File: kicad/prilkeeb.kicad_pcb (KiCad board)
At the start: 2 copper layers, 162.4 x 143.1 mm, 71 parts, among them U2 Nice_Nano_V2

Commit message: Update layout
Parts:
- added REF**: Stabilizer_MX_2.00u, ScottoKeebs_Stabilizer:Stabilizer_MX_2.00u, F.Cu at (142.2, 156.1)
- D1, D10, D11, D12, D13, D14, D15, D16, D17, D18, D19, D2, D20, D21, D22, D23, D24, D25, D26, D27, D28, D29, D3, D30, D31, D32, D33, D34, D35, D4, D5, D6, D7, D8, D9: moved to B.Cu
- moved S33 48.0 mm to (142.2, 156.1), turned to -30 degrees
- moved D33 44.1 mm to (158.9, 178.7), turned to 60 degrees
- moved S35 39.7 mm to (156.0, 173.5), turned to -30 degrees
- moved D32 28.8 mm to (121.3, 159.9), turned to 60 degrees
- moved S32 25.6 mm to (118.4, 154.8), turned to -30 degrees
- moved D34 20.4 mm to (168.4, 162.2), turned to 60 degrees
- moved S19 19.1 mm to (38.1, 104.8), turned to 0 degrees
- moved S20 19.1 mm to (57.1, 104.8), turned to 0 degrees
- moved S12 19.0 mm to (38.1, 85.7), turned to 0 degrees
- moved S13 19.0 mm to (57.1, 85.7), turned to 0 degrees
- moved S26 19.0 mm to (38.1, 123.8), turned to 0 degrees
- moved S27 19.0 mm to (57.1, 123.8), turned to 0 degrees
- moved S29 19.0 mm to (38.1, 142.9), turned to 0 degrees
- moved S30 19.0 mm to (57.1, 142.9), turned to 0 degrees
- moved S31 19.0 mm to (76.2, 142.9), turned to 0 degrees
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- renumbered S3 to S1, S12 to S10, S13 to S11, S8 to S12, S9 to S13, S17 to S15, S18 to S16, S19 to S17, S20 to S18, S15 to S19, S4 to S2, S16 to S20, S24 to S22, S25 to S23, S26 to S24, S27 to S25, S22 to S26, S23 to S27, S5 to S3, S35 to S33, S33 to S35, S6 to S4, S1 to S5, S2 to S6, S10 to S8, S11 to S9
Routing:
- net Col_1: track 247.7 -> 0.00 mm
- net Col_2: track 226.2 -> 0.00 mm
- net Row_5: track 210.0 -> 0.00 mm
- net Col_4: track 200.5 -> 0.00 mm
- net Col_5: track 167.3 -> 0.00 mm
- net Col_3: track 208.5 -> 44.4 mm
- net Row_2: track 151.8 -> 0.00 mm
- net Row_4: track 190.9 -> 45.1 mm
- net Col_6: track 142.6 -> 0.00 mm
- net Row_1: track 138.9 -> 0.00 mm
- net Row_3: track 172.5 -> 36.4 mm
- net Col_7: track 104.9 -> 0.00 mm
- net Net-(D12-A): track 14.1 -> 0.00 mm
- net Net-(D22-A): track 12.4 -> 0.00 mm
- net Net-(D1-A): track 12.3 -> 0.00 mm
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
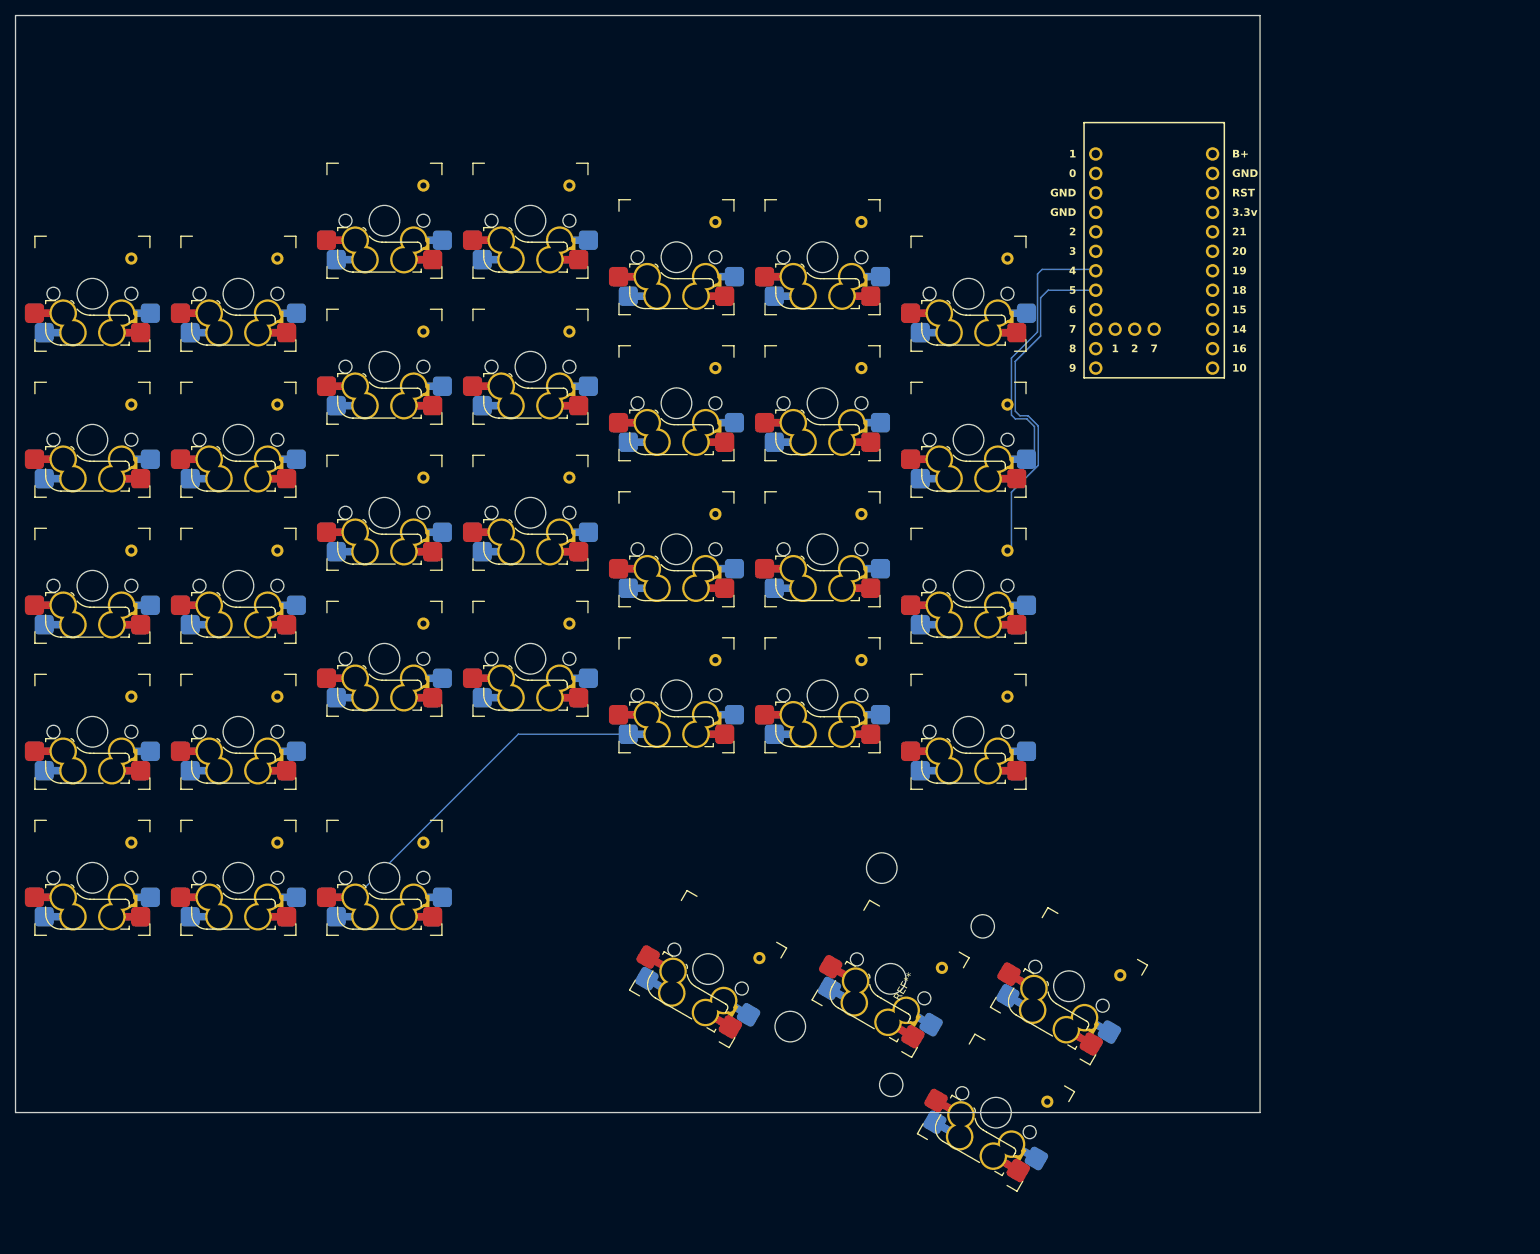
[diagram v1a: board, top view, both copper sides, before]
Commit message: Update placement and basice routing
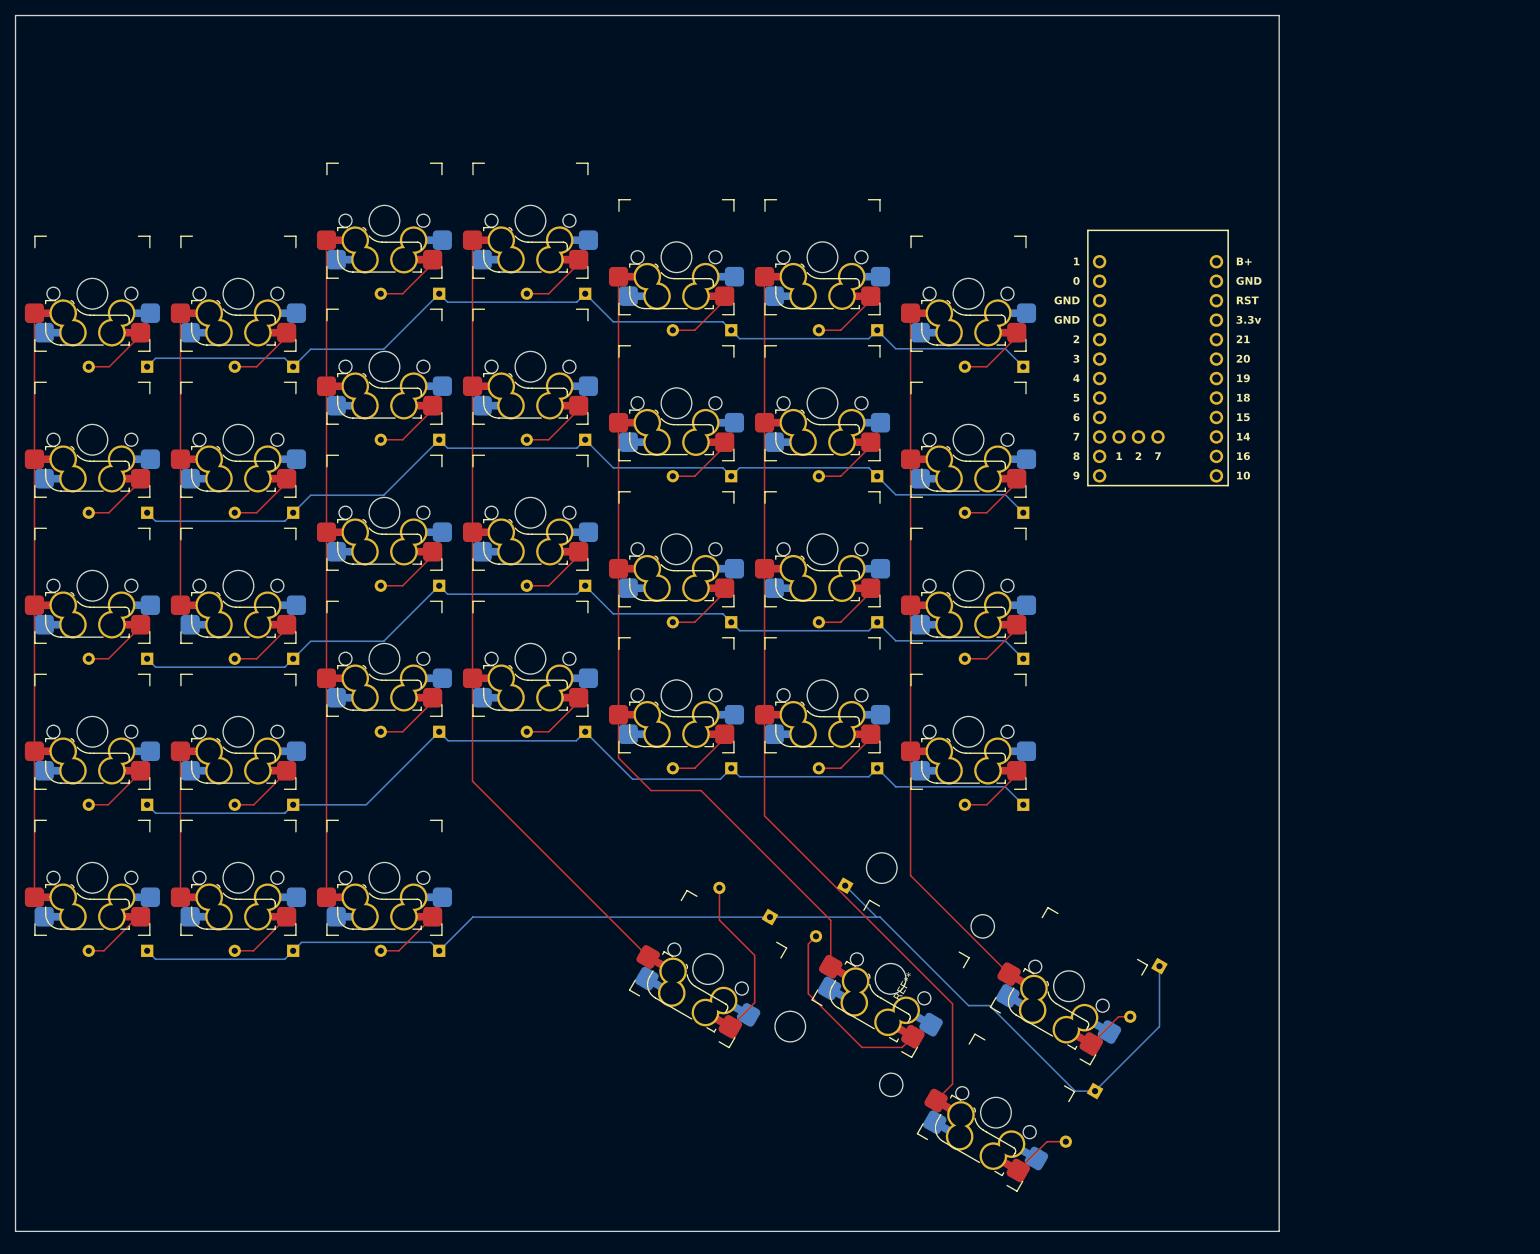
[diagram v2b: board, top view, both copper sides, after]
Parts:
- moved D35 41.5 mm to (136.3, 143.9), turned to -120 degrees
- moved D34 32.9 mm to (177.3, 154.4), turned to -120 degrees
- moved S34 23.3 mm to (165.5, 157.0)
- moved S33 22.2 mm to (142.2, 156.1)
- moved S35 19.1 mm to (156.0, 173.5)
- moved U2 14.1 mm to (177.1, 76.2)
- moved D32 13.0 mm to (126.5, 148.0), turned to 150 degrees
- moved D33 8.53 mm to (168.9, 170.7), turned to -120 degrees
- moved D2 6.81 mm to (64.3, 76.2), turned to 180 degrees
- moved D30 6.81 mm to (64.3, 152.4), turned to 180 degrees
- moved D9 6.81 mm to (64.3, 95.2), turned to 180 degrees
- moved D14 6.81 mm to (159.5, 95.2), turned to 180 degrees
- moved D17 6.81 mm to (83.3, 104.8), turned to 180 degrees
- moved D18 6.81 mm to (102.4, 104.8), turned to 180 degrees
- moved D24 6.81 mm to (83.3, 123.8), turned to 180 degrees
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- renumbered D34 to D33, D35 to D34, D33 to D35, S35 to S33, S33 to S34, S34 to S35
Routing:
- net Row_5: track 0.00 -> 162.3 mm
- net Row_1: track 0.00 -> 125.3 mm
- net Row_2: track 0.00 -> 124.9 mm
- net Col_6: track 0.00 -> 119.3 mm
- net Col_5: track 0.00 -> 106.9 mm
- net Col_4: track 0.00 -> 103.0 mm
- net Col_7: track 0.00 -> 91.5 mm
- net Row_3: track 36.4 -> 124.9 mm
- net Row_4: track 45.1 -> 126.2 mm
- net Col_1: track 0.00 -> 76.2 mm
- net Col_2: track 0.00 -> 57.1 mm
- net Col_3: track 44.4 -> 85.7 mm
- net Net-(D35-A): track 0.00 -> 25.6 mm
- net Net-(D32-A): track 0.00 -> 21.4 mm
- net Net-(D29-A): track 0.00 -> 14.1 mm
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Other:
- board size 162.4 x 143.1 mm -> 164.9 x 158.6 mm

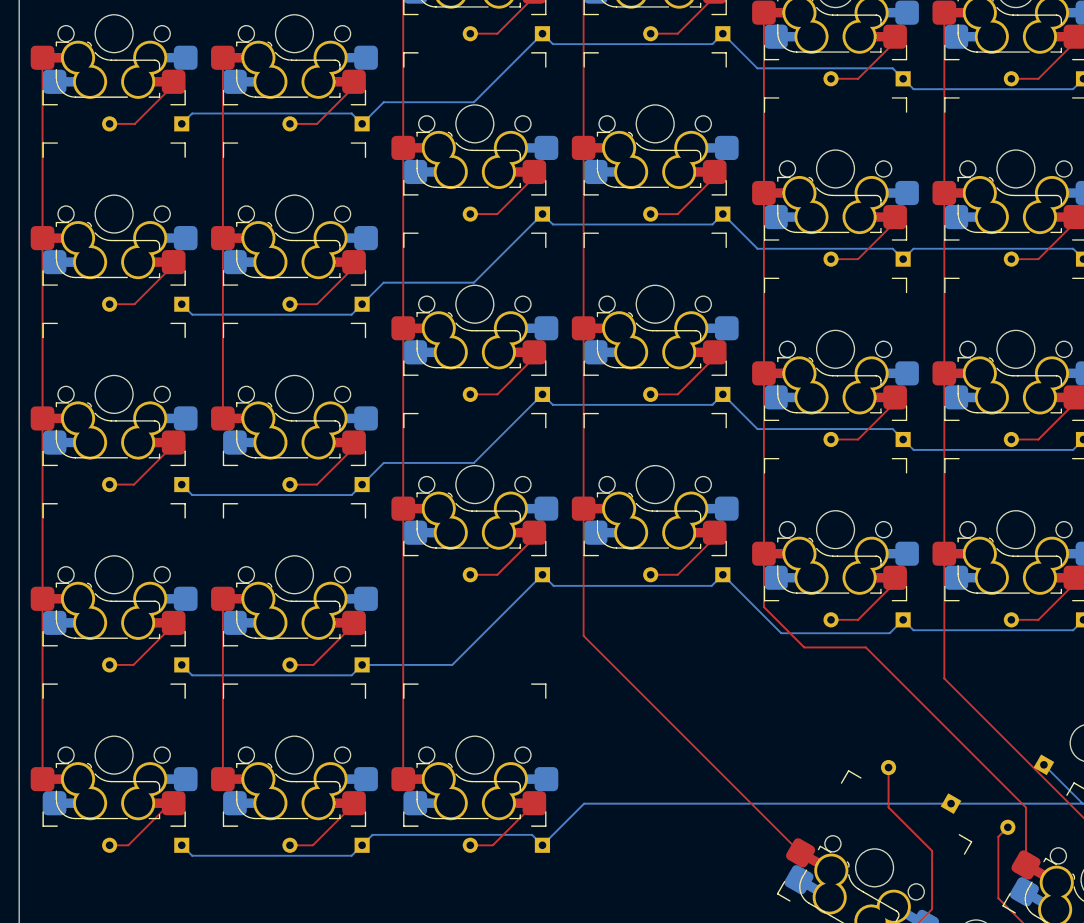
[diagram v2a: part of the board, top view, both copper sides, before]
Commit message: Update project name
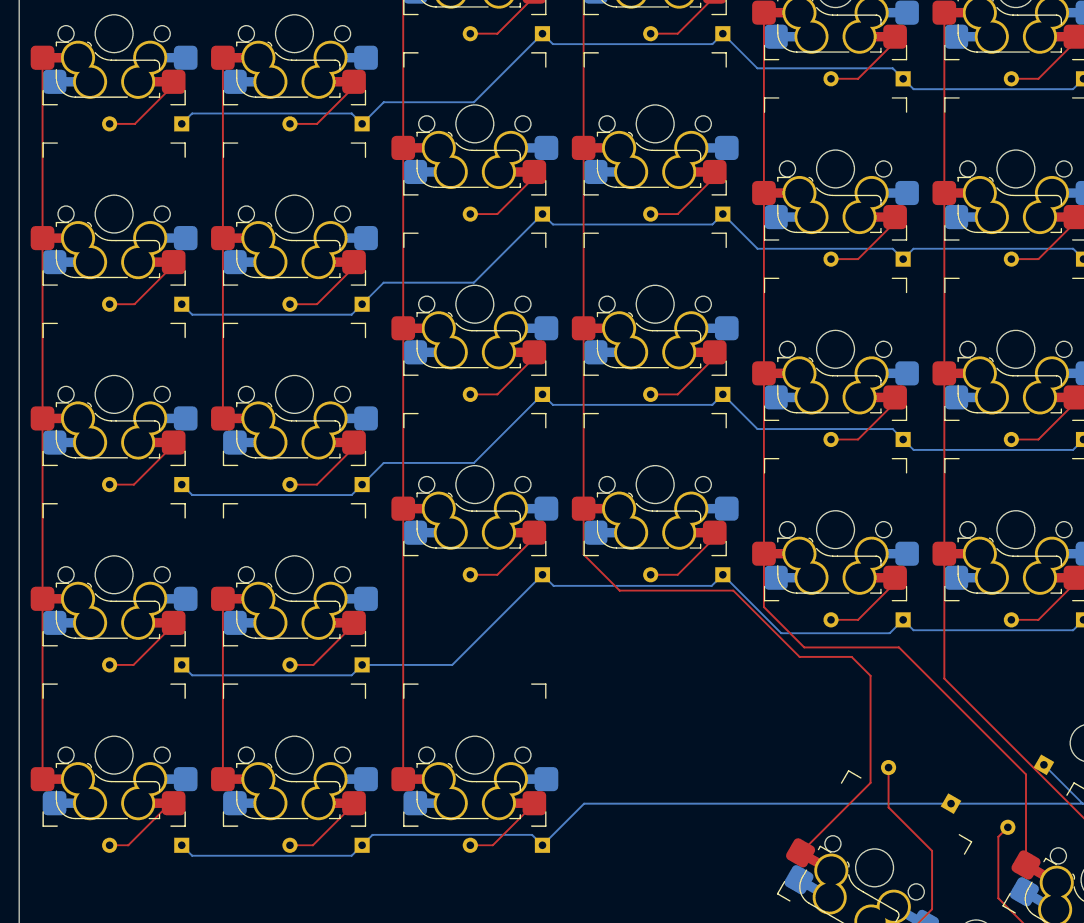
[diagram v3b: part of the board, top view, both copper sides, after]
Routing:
- net Col_4: track 103.0 -> 119.4 mm
- net Col_5: track 106.9 -> 108.9 mm
- net Col_1: track 76.2 -> 77.9 mm
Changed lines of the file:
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@@
+	)
+	(segment
+		(start 30.54 69.215)
+		(end 32.285 69.215)
+		(width 0.2)
+		(layer "F.Cu")
+		(net 41)
 	)
 	(segment
@@
 	)
 	(segment
-		(start 87.69 130.283661)
-		(end 110.607294 153.200955)
+		(start 103.5 125.5)
+		(end 110.5 132.5)
 		(width 0.2)
 		(layer "F.Cu")
@@
 	)
 	(segment
+		(start 87.69 121.69)
+		(end 91.5 125.5)
+		(width 0.2)
+		(layer "F.Cu")
+		(net 44)
+	)
+	(segment
+		(start 87.69 116.84)
+		(end 87.69 121.69)
+		(width 0.2)
+		(layer "F.Cu")
+		(net 44)
+	)
+	(segment
+		(start 91.5 125.5)
+		(end 103.5 125.5)
+		(width 0.2)
+		(layer "F.Cu")
+		(net 44)
+	)
+	(segment
 		(start 87.69 59.69)
 		(end 87.69 78.74)
@@
 	)
 	(segment
-		(start 87.69 116.84)
-		(end 87.69 130.283661)
+		(start 116 132.5)
+		(end 118 134.5)
+		(width 0.2)
+		(layer "F.Cu")
+		(net 44)
+	)
+	(segment
+		(start 110.5 132.5)
+		(end 116 132.5)
+		(width 0.2)
+		(layer "F.Cu")
+		(net 44)
+	)
+	(segment
+		(start 118 134.5)
+		(end 118 145.808249)
+		(width 0.2)
+		(layer "F.Cu")
+		(net 44)
+	)
+	(segment
+		(start 118 145.808249)
+		(end 110.607294 153.200955)
 		(width 0.2)
 		(layer "F.Cu")
@@
 	)
 	(segment
-		(start 117.5 131.5)
-		(end 134.419794 148.419794)
-		(width 0.2)
-		(layer "F.Cu")
-		(net 45)
-	)
-	(segment
-		(start 134.419794 148.419794)
-		(end 134.419794 154.477063)
-		(width 0.2)
-		(layer "F.Cu")
-		(net 45)
-	)
-	(segment
-		(start 111 131.5)
-		(end 117.5 131.5)
+		(start 121 131.5)
+		(end 134.419794 144.919794)
 		(width 0.2)
 		(layer "F.Cu")
@@
 		(width 0.2)
 		(layer "F.Cu")
+		(net 45)
+	)
+	(segment
+		(start 111 131.5)
+		(end 121 131.5)
+		(width 0.2)
+		(layer "F.Cu")
+		(net 45)
+	)
+	(segment
+		(start 134.419794 144.919794)
+		(end 134.419794 154.477063)
+		(width 0.2)
+		(layer "F.Cu")

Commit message: Acceptable tracks
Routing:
- net Col_2: track 57.1 -> 240.0 mm
- net Col_1: track 77.9 -> 259.5 mm
- net Col_3: track 85.7 -> 226.6 mm
- net Row_5: track 162.3 -> 286.7 mm
- net Col_4: track 119.4 -> 232.5 mm
- net Col_5: track 108.9 -> 210.9 mm
- net Col_6: track 119.3 -> 208.6 mm
- net Col_7: track 91.5 -> 167.7 mm
- net Row_4: track 126.2 -> 194.4 mm
- net Row_3: track 124.9 -> 175.5 mm
- net Row_2: track 124.9 -> 161.1 mm
- net Row_1: track 125.3 -> 136.8 mm
- net Net-(D34-A): track 6.56 -> 3.55 mm

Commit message: Nearly finish the routing
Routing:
- net Row_2: track 161.1 -> 175.6 mm
- net Col_6: track 208.6 -> 222.7 mm, vias 0 -> 2
- net Row_1: track 136.8 -> 147.9 mm
- net Col_4: track 232.5 -> 223.5 mm, vias 0 -> 2
- net Row_4: track 194.4 -> 185.9 mm
- net Col_3: track 226.6 -> 219.5 mm, vias 0 -> 1
- net Col_5: track 210.9 -> 217.6 mm, vias 0 -> 4
- net Col_2: track 240.0 -> 235.3 mm, vias 0 -> 1
- net Row_5: track 286.7 -> 282.6 mm, vias 0 -> 3
- net Col_1: track 259.5 -> 256.1 mm, vias 0 -> 1
- net Row_3: track 175.5 -> 178.0 mm

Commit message: Update layout
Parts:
- added REF**: Stabilizer_MX_2.00u, ScottoKeebs_Stabilizer:Stabilizer_MX_2.00u, F.Cu at (176.6, 167.2)
- moved D33 40.4 mm to (148.1, 136.0), turned to 180 degrees
- moved D34 25.5 mm to (159.6, 136.0), turned to 180 degrees
- moved U2 21.0 mm to (198.1, 76.1)
- moved S11 19.1 mm to (152.4, 81.0)
- moved S18 19.1 mm to (152.4, 100.0)
- moved S25 19.1 mm to (152.4, 119.1)
- moved S4 19.1 mm to (152.4, 61.9)
- moved S13 19.1 mm to (76.2, 85.7)
- moved S20 19.1 mm to (76.2, 104.8)
- moved S27 19.1 mm to (76.2, 123.8)
- moved S30 19.1 mm to (76.2, 142.9)
- moved S6 19.1 mm to (76.2, 66.7)
- moved S1 19.0 mm to (95.2, 57.1)
- moved S10 19.0 mm to (133.3, 81.0)
- moved S15 19.0 mm to (95.2, 95.2)
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- renumbered S35 to S32, S34 to S33, S32 to S34, S33 to S35
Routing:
- net Row_5: track 282.6 -> 0.00 mm, vias 3 -> 0
- net Col_1: track 256.1 -> 17.5 mm, vias 1 -> 0
- net Col_2: track 235.3 -> 0.00 mm, vias 1 -> 0
- net Col_4: track 223.5 -> 0.00 mm, vias 2 -> 0
- net Col_6: track 222.7 -> 0.00 mm, vias 2 -> 0
- net Col_3: track 219.5 -> 0.00 mm, vias 1 -> 0
- net Col_5: track 217.6 -> 0.00 mm, vias 4 -> 0
- net Row_4: track 185.9 -> 0.00 mm
- net Row_3: track 178.0 -> 0.00 mm
- net Row_2: track 175.6 -> 0.00 mm
- net Col_7: track 167.2 -> 0.00 mm
- net Row_1: track 147.9 -> 0.00 mm
- net Net-(D35-A): track 25.6 -> 0.00 mm
- net Net-(D32-A): track 21.4 -> 0.00 mm
- net Net-(D29-A): track 14.1 -> 0.00 mm
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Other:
- board size 164.9 x 158.6 mm -> 196.9 x 158.6 mm

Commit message: Routing
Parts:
-  : renamed from REF** (x2)
- moved D34 15.7 mm to (175.3, 136.5)
- moved D32 10.8 mm to (118.3, 128.0)
- moved D33 8.91 mm to (156.3, 132.5)
- moved D35 3.50 mm to (137.1, 132.5)
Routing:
- net Col_1: track 17.5 -> 277.5 mm, vias 0 -> 1
- net Col_3: track 0.00 -> 245.0 mm, vias 0 -> 1
- net Col_2: track 0.00 -> 242.9 mm, vias 0 -> 1
- net Col_4: track 0.00 -> 240.2 mm, vias 0 -> 1
- net Col_5: track 0.00 -> 227.8 mm, vias 0 -> 1
- net Col_6: track 0.00 -> 205.6 mm, vias 0 -> 1
- net Row_5: track 0.00 -> 205.5 mm
- net Col_7: track 0.00 -> 200.9 mm, vias 0 -> 1
- net Row_4: track 0.00 -> 198.1 mm
- net Row_3: track 0.00 -> 181.4 mm
- net Row_2: track 0.00 -> 161.9 mm
- net Row_1: track 0.00 -> 149.1 mm
- net Net-(D34-A): track 0.00 -> 47.1 mm
- net Net-(D33-A): track 0.00 -> 43.9 mm
- net Net-(D35-A): track 0.00 -> 43.5 mm
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
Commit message: Update layout
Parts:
- moved D29 43.5 mm to (99.0, 132.0)
- moved D30 30.9 mm to (99.0, 128.0)
- moved D31 27.6 mm to (118.1, 132.5)
- moved S35 25.8 mm to (144.3, 162.3), turned to -12 degrees
- moved S32 19.1 mm to (148.3, 143.7), turned to -12 degrees
- moved   9.41 mm to (183.6, 160.9), turned to 78 degrees
- moved S34 9.41 mm to (183.6, 160.9), turned to -12 degrees
- moved D22 7.18 mm to (61.0, 133.3)
- moved   6.04 mm to (164.9, 157.0), turned to -102 degrees
- moved S33 6.04 mm to (164.9, 157.0), turned to -12 degrees
- moved U2 4.69 mm to (194.5, 73.1)
- moved D32 0.19 mm to (118.1, 128.0)
- renumbered S35 to S32, S32 to S33, S33 to S34, S34 to S35
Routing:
- net Col_1: track 277.5 -> 0.00 mm, vias 1 -> 0
- net Col_3: track 245.0 -> 0.00 mm, vias 1 -> 0
- net Col_2: track 242.9 -> 0.00 mm, vias 1 -> 0
- net Col_4: track 240.2 -> 0.00 mm, vias 1 -> 0
- net Col_5: track 227.8 -> 0.00 mm, vias 1 -> 0
- net Col_6: track 205.6 -> 0.00 mm, vias 1 -> 0
- net Row_5: track 205.5 -> 0.00 mm
- net Col_7: track 200.9 -> 0.00 mm, vias 1 -> 0
- net Row_4: track 198.1 -> 0.00 mm
- net Row_3: track 181.4 -> 0.00 mm
- net Row_2: track 161.9 -> 0.00 mm
- net Row_1: track 149.1 -> 0.00 mm
- net Net-(D34-A): track 47.1 -> 0.00 mm
- net Net-(D33-A): track 43.9 -> 0.00 mm
- net Net-(D35-A): track 43.5 -> 0.00 mm
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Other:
- board size 196.9 x 158.6 mm -> 176.5 x 142.7 mm
